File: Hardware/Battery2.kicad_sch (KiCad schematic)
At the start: 67 parts

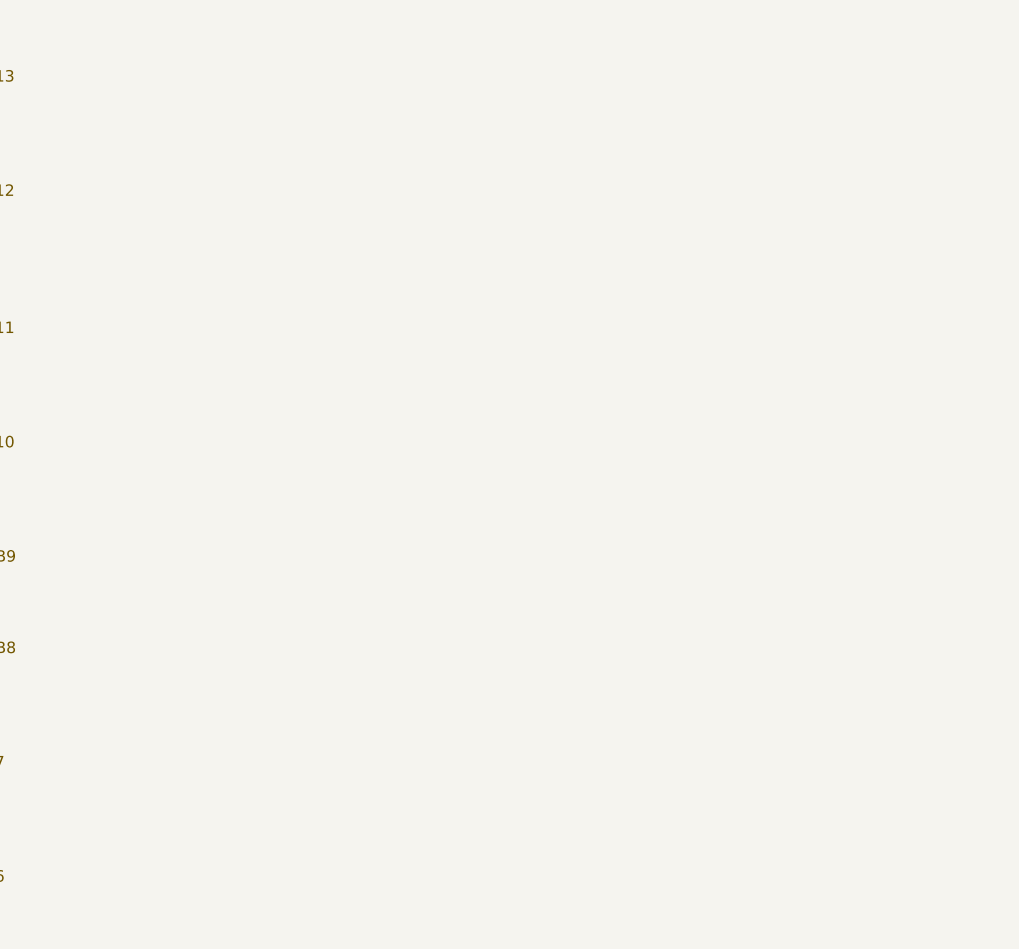
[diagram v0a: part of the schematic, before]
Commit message: Dodano wyjaśnienia w schemacie, zmieniono nazewnictwo wewnętrzne lini can
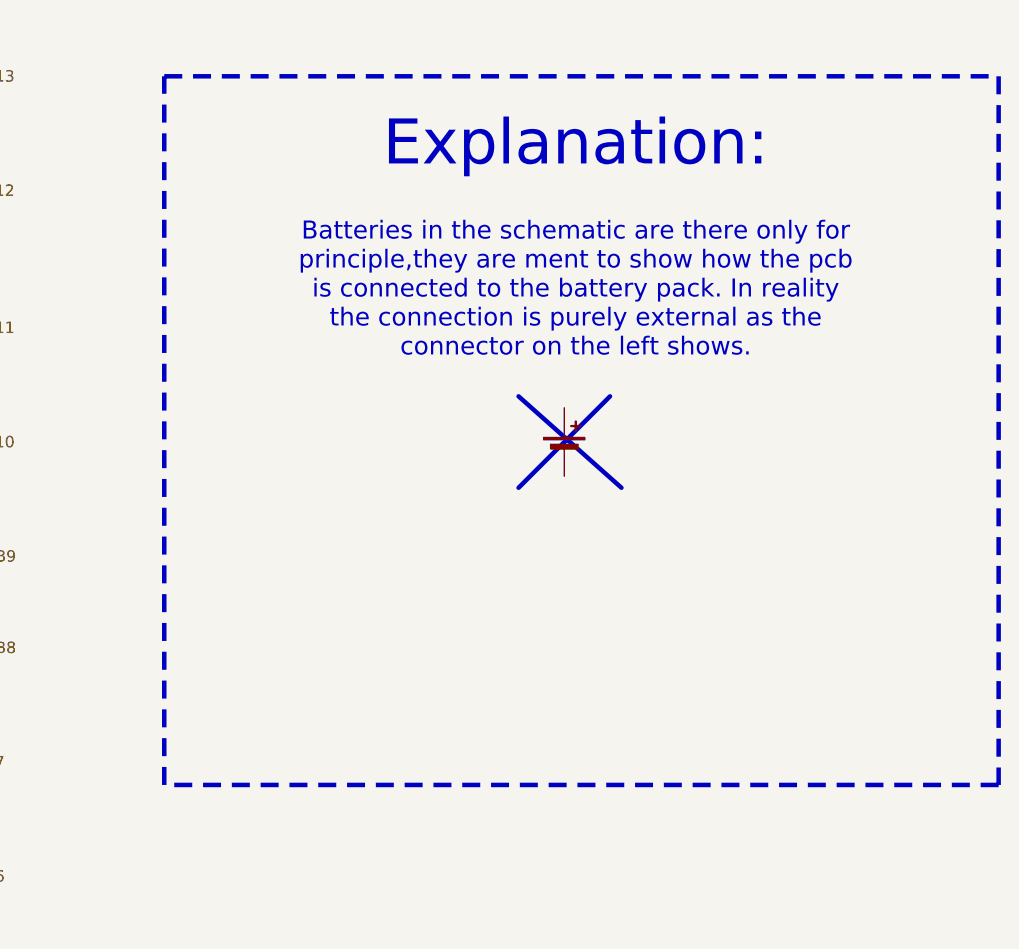
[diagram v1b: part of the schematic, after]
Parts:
- added BT28: Battery_Cell, symbol Device:Battery_Cell
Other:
- note added: "Batteries in the schematic are there only for principle,they are ment to show how the pcb is connected to the battery pack. In reality the connection is purely external as the connector on the left shows."
- note added: "Explanation:"
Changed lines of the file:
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@@
 	(generator_version "9.0")
 	(paper "A4")
+	(rectangle
+		(start 186.69 19.05)
+		(end 279.4 97.79)
+		(stroke
+			(width 0.5)
+			(type dash)
+			(color 0 0 0 1)
+		)
+		(fill
+			(type none)
+		)
+	)
 	(text "'GND_HV2' is connected via 'Batt_coupling' to cell number 13 and serves as a ground for 2nd ltc"
 		(exclude_from_sim no)
@@
 		)
 	)
+	(text "Batteries in the schematic are there only for \nprinciple,they are ment to show how the pcb \nis connected to the battery pack. In reality\nthe connection is purely external as the\nconnector on the left shows. \n\n"
+		(exclude_from_sim no)
+		(at 232.41 44.45 0)
+		(effects
+			(font
+				(size 2 2)
+				(color 0 0 0 1)
+			)
+		)
+	)
+	(text "Explanation:"
+		(exclude_from_sim no)
+		(at 232.41 26.67 0)
+		(effects
+			(font
+				(size 5 5)
+				(thickness 0.625)
+				(color 0 0 0 1)
+			)
+		)
+	)
 	(junction
 		(at 154.94 171.45)
@@
 		)
 	)
+	(polyline
+		(pts
+			(xy 226.06 54.61) (xy 237.49 64.77)
+		)
+		(stroke
+			(width 0.5)
+			(type solid)
+			(color 255 0 0 1)
+		)
+	)
 	(wire
 		(pts
@@
 		)
 	)
+	(polyline
+		(pts
+			(xy 226.06 64.77) (xy 236.22 54.61)
+		)
+		(stroke
+			(width 0.5)
+			(type solid)
+			(color 255 0 0 1)
+		)
+	)
 	(wire
 		(pts
@@
 					(unit 1)
 				)
+			)
+		)
+	)
+	(symbol
+		(lib_id "Device:Battery_Cell")
+		(at 231.14 60.96 0)
+		(unit 1)
+		(exclude_from_sim no)
+		(in_bom no)
+		(on_board no)
+		(dnp no)
+		(fields_autoplaced yes)
+		(property "Reference" "BT28"
+			(at 234.95 57.8484 0)
+			(effects
+				(font
+					(size 1.27 1.27)
+				)
+				(justify left)
+				(hide yes)
+			)
+		)
+		(property "Value" "Battery_Cell"
+			(at 234.95 60.3884 0)
+			(effects
+				(font
+					(size 1.27 1.27)
+				)
+				(justify left)
+				(hide yes)
+			)
+		)
+		(property "Footprint" ""
+			(at 231.14 59.436 90)
+			(effects
+				(font
+					(size 1.27 1.27)
+				)
+				(hide yes)
+			)
+		)
+		(property "Datasheet" "~"
+			(at 231.14 59.436 90)
+			(effects
+				(font
+					(size 1.27 1.27)
+				)
+				(hide yes)
+			)
+		)
+		(property "Description" "Single-cell battery"
+			(at 231.14 60.96 0)
+			(effects
+				(font
+					(size 1.27 1.27)
+				)
+				(hide yes)
+			)
+		)
+		(pin "1"
+		)
+		(pin "2"
+		)
+		(instances
+			(project "BMS"
+				(path "/26289bb6-56bc-4ca1-b1a2-18d58d1afdf5/99f7ea83-6836-44ea-889b-f0d453e84b38/3dcd8643-765f-4aab-99d6-4ed68d4de44f"
+					(reference "BT28")
+					(unit 1)
+				)
